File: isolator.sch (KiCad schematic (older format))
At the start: 0 parts

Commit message: Added library for project specific symbols
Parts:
- added U?: Si8640BA-B-IU, Package_SO:QSOP-16_3.9x4.9mm_P0.635mm, symbol Isolator:Si8640BA-B-IU
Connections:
- net labels added: IN1, IN2, IN3, IN4, IN5, IN6, OUT1, OUT2, OUT3, OUT4, OUT5, OUT6
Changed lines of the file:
@@
 Comment4 ""
 $EndDescr
+$Comp
+L Isolator:Si8640BA-B-IU U?
+U 1 1 5BCC634E
+P 5350 3650
+F 0 "U?" H 5350 4317 50  0000 C CNN
+F 1 "Si8640BA-B-IU" H 5350 4226 50  0000 C CNN
+F 2 "Package_SO:QSOP-16_3.9x4.9mm_P0.635mm" H 5350 3100 50  0001 C CIN
+F 3 "https://www.silabs.com/documents/public/data-sheets/si864x-datasheet.pdf" H 5350 4050 50  0001 C CNN
+	1    5350 3650
+	1    0    0    -1
+$EndComp
+Text HLabel 3650 3350 0    50   Input ~ 0
+IN1
+Text HLabel 3650 3450 0    50   Input ~ 0
+IN2
+Text HLabel 3650 3550 0    50   Input ~ 0
+IN3
+Text HLabel 3650 3650 0    50   Input ~ 0
+IN4
+Text HLabel 3650 3750 0    50   Input ~ 0
+IN5
+Text HLabel 3650 3850 0    50   Input ~ 0
+IN6
+Text HLabel 6850 3250 2    50   Output ~ 0
+OUT1
+Text HLabel 6850 3350 2    50   Output ~ 0
+OUT2
+Text HLabel 6850 3450 2    50   Output ~ 0
+OUT3
+Text HLabel 6850 3550 2    50   Output ~ 0
+OUT4
+Text HLabel 6850 3650 2    50   Output ~ 0
+OUT5
+Text HLabel 6850 3750 2    50   Output ~ 0
+OUT6
 $EndSCHEMATC

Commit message: Added isolators and RJ-45 connectors
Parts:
- removed U?: Si8640BA-B-IU, Package_SO:QSOP-16_3.9x4.9mm_P0.635mm, symbol Isolator:Si8640BA-B-IU
- added U?: Si8640BB-B-IS1, Package_SO:SOIC-16_3.9x9.9mm_P1.27mm, symbol Isolator:Si8640BB-B-IS1
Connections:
- net labels added: +3V3, +5V, GNDREF
- net labels removed: IN5, IN6, OUT5, OUT6
- wire segments 0 -> 18
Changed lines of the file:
@@
 $Descr A4 11693 8268
 encoding utf-8
-Sheet 3 5
+Sheet 6 8
 Title ""
 Date ""
@@
 Comment4 ""
 $EndDescr
+Text HLabel 4400 3400 0    50   Input ~ 0
+IN1
+Text HLabel 4400 3500 0    50   Input ~ 0
+IN2
+Text HLabel 4400 3600 0    50   Input ~ 0
+IN3
+Text HLabel 4400 3700 0    50   Input ~ 0
+IN4
+Text HLabel 5950 3400 2    50   Output ~ 0
+OUT1
+Text HLabel 5950 3500 2    50   Output ~ 0
+OUT2
+Text HLabel 5950 3600 2    50   Output ~ 0
+OUT3
+Text HLabel 5950 3700 2    50   Output ~ 0
+OUT4
 $Comp
-L Isolator:Si8640BA-B-IU U?
-U 1 1 5BCC634E
-P 5350 3650
-F 0 "U?" H 5350 4317 50  0000 C CNN
-F 1 "Si8640BA-B-IU" H 5350 4226 50  0000 C CNN
-F 2 "Package_SO:QSOP-16_3.9x4.9mm_P0.635mm" H 5350 3100 50  0001 C CIN
-F 3 "https://www.silabs.com/documents/public/data-sheets/si864x-datasheet.pdf" H 5350 4050 50  0001 C CNN
-	1    5350 3650
+L Isolator:Si8640BB-B-IS1 U?
+U 1 1 5BCC7CBC
+P 5200 3500
+AR Path="/5BCC578B/5BCC7CBC" Ref="U?"  Part="1"
+AR Path="/5BCC79AE/5BCC7CBC" Ref="U?"  Part="1"
+F 0 "U?" H 5200 4167 50  0000 C CNN
+F 1 "Si8640BB-B-IS1" H 5200 4076 50  0000 C CNN
+F 2 "Package_SO:SOIC-16_3.9x9.9mm_P1.27mm" H 5200 2950 50  0001 C CIN
+F 3 "https://www.silabs.com/documents/public/data-sheets/si864x-datasheet.pdf" H 5200 3900 50  0001 C CNN
+	1    5200 3500
 	1    0    0    -1
 $EndComp
-Text HLabel 3650 3350 0    50   Input ~ 0
-IN1
-Text HLabel 3650 3450 0    50   Input ~ 0
-IN2
-Text HLabel 3650 3550 0    50   Input ~ 0
-IN3
-Text HLabel 3650 3650 0    50   Input ~ 0
-IN4
-Text HLabel 3650 3750 0    50   Input ~ 0
-IN5
-Text HLabel 3650 3850 0    50   Input ~ 0
-IN6
-Text HLabel 6850 3250 2    50   Output ~ 0
-OUT1
-Text HLabel 6850 3350 2    50   Output ~ 0
-OUT2
-Text HLabel 6850 3450 2    50   Output ~ 0
-OUT3
-Text HLabel 6850 3550 2    50   Output ~ 0
-OUT4
-Text HLabel 6850 3650 2    50   Output ~ 0
-OUT5
-Text HLabel 6850 3750 2    50   Output ~ 0
-OUT6
+$Comp
+L power:GNDREF #PWR?
+U 1 1 5BCC7D47
+P 4650 4100
+AR Path="/5BCC578B/5BCC7D47" Ref="#PWR?"  Part="1"
+AR Path="/5BCC79AE/5BCC7D47" Ref="#PWR?"  Part="1"
+F 0 "#PWR?" H 4650 3850 50  0001 C CNN
+F 1 "GNDREF" H 4655 3927 50  0000 C CNN
+F 2 "" H 4650 4100 50  0001 C CNN
+F 3 "" H 4650 4100 50  0001 C CNN
+	1    4650 4100
+	1    0    0    -1
+$EndComp
+$Comp
+L power:GNDREF #PWR?
+U 1 1 5BCC7D5B
+P 5750 4100
+AR Path="/5BCC578B/5BCC7D5B" Ref="#PWR?"  Part="1"
+AR Path="/5BCC79AE/5BCC7D5B" Ref="#PWR?"  Part="1"
+F 0 "#PWR?" H 5750 3850 50  0001 C CNN
+F 1 "GNDREF" H 5755 3927 50  0000 C CNN
+F 2 "" H 5750 4100 50  0001 C CNN
+F 3 "" H 5750 4100 50  0001 C CNN
+	1    5750 4100
+	1    0    0    -1
+$EndComp
+$Comp
+L power:+3V3 #PWR?
+U 1 1 5BCC7DB8
+P 4650 2950
+AR Path="/5BCC578B/5BCC7DB8" Ref="#PWR?"  Part="1"
+AR Path="/5BCC79AE/5BCC7DB8" Ref="#PWR?"  Part="1"
+F 0 "#PWR?" H 4650 2800 50  0001 C CNN
+F 1 "+3V3" H 4665 3123 50  0000 C CNN
+F 2 "" H 4650 2950 50  0001 C CNN
+F 3 "" H 4650 2950 50  0001 C CNN
+	1    4650 2950
+	1    0    0    -1
+$EndComp
+$Comp
+L power:+5V #PWR?
+U 1 1 5BCC7E07
+P 5750 2950
+AR Path="/5BCC578B/5BCC7E07" Ref="#PWR?"  Part="1"
+AR Path="/5BCC79AE/5BCC7E07" Ref="#PWR?"  Part="1"
+F 0 "#PWR?" H 5750 2800 50  0001 C CNN
+F 1 "+5V" H 5765 3123 50  0000 C CNN
+F 2 "" H 5750 2950 50  0001 C CNN
+F 3 "" H 5750 2950 50  0001 C CNN
+	1    5750 2950
+	1    0    0    -1
+$EndComp
+Wire Wire Line
+	5600 3100 5750 3100
+Wire Wire Line
+	5600 3200 5750 3200
+Wire Wire Line
+	5750 3200 5750 3100
+Connection ~ 5750 3100
+Wire Wire Line
+	5600 3400 5950 3400
+Wire Wire Line
+	5950 3500 5600 3500
+Wire Wire Line
+	5600 3600 5950 3600
+Wire Wire Line
+	5600 3700 5950 3700
+Wire Wire Line
+	5600 3900 5750 3900
+Wire Wire Line
+	5750 3900 5750 4100
+Wire Wire Line
+	4800 3100 4650 3100
+Wire Wire Line
+	4650 3100 4650 2950
+Wire Wire Line
+	4650 4100 4650 3900
+Wire Wire Line
+	4650 3900 4800 3900
+Wire Wire Line
+	4800 3700 4400 3700
+Wire Wire Line
+	4400 3600 4800 3600
+Wire Wire Line
+	4800 3500 4400 3500
+Wire Wire Line
+	4400 3400 4800 3400
+Wire Wire Line
+	5750 2950 5750 3100
 $EndSCHEMATC

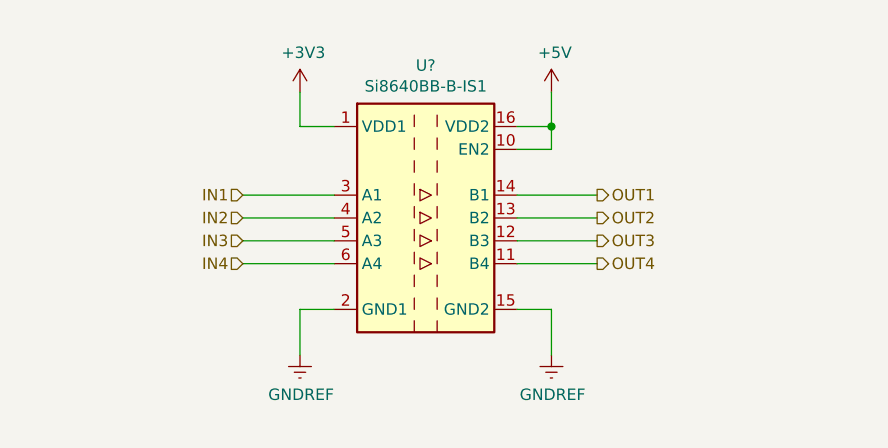
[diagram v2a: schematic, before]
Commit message: Added charge pump IC REG71050
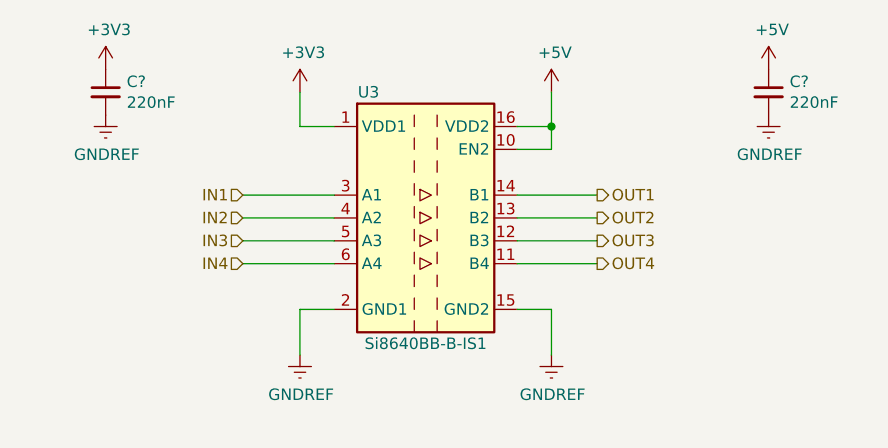
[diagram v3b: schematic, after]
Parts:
- added C? (x2): 220nF, symbol Device:C_Small
- gave numbers to parts that had none: 1
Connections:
- net +3V3: now also C?.1
- net +5V: now also C?.1
- net GNDREF: now also C?.2, C?.2
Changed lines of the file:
@@
 $Descr A4 11693 8268
 encoding utf-8
-Sheet 6 8
+Sheet 6 11
 Title ""
 Date ""
@@
 OUT4
 $Comp
-L Isolator:Si8640BB-B-IS1 U?
+L Isolator:Si8640BB-B-IS1 U1
 U 1 1 5BCC7CBC
 P 5200 3500
-AR Path="/5BCC578B/5BCC7CBC" Ref="U?"  Part="1"
-AR Path="/5BCC79AE/5BCC7CBC" Ref="U?"  Part="1"
-F 0 "U?" H 5200 4167 50  0000 C CNN
-F 1 "Si8640BB-B-IS1" H 5200 4076 50  0000 C CNN
+AR Path="/5BCC578B/5BCC7CBC" Ref="U1"  Part="1"
+AR Path="/5BCC79AE/5BCC7CBC" Ref="U3"  Part="1"
+AR Path="/5BCC7A96/5BCC7CBC" Ref="U2"  Part="1"
+AR Path="/5BCC8BB7/5BCC7CBC" Ref="U4"  Part="1"
+F 0 "U3" H 4950 4050 50  0000 C CNN
+F 1 "Si8640BB-B-IS1" H 5200 2950 50  0000 C CNN
 F 2 "Package_SO:SOIC-16_3.9x9.9mm_P1.27mm" H 5200 2950 50  0001 C CIN
 F 3 "https://www.silabs.com/documents/public/data-sheets/si864x-datasheet.pdf" H 5200 3900 50  0001 C CNN
@@
 $EndComp
 $Comp
-L power:GNDREF #PWR?
+L power:GNDREF #PWR0105
 U 1 1 5BCC7D47
 P 4650 4100
-AR Path="/5BCC578B/5BCC7D47" Ref="#PWR?"  Part="1"
-AR Path="/5BCC79AE/5BCC7D47" Ref="#PWR?"  Part="1"
-F 0 "#PWR?" H 4650 3850 50  0001 C CNN
+AR Path="/5BCC578B/5BCC7D47" Ref="#PWR0105"  Part="1"
+AR Path="/5BCC79AE/5BCC7D47" Ref="#PWR0118"  Part="1"
+AR Path="/5BCC7A96/5BCC7D47" Ref="#PWR0114"  Part="1"
+AR Path="/5BCC8BB7/5BCC7D47" Ref="#PWR0122"  Part="1"
+F 0 "#PWR0118" H 4650 3850 50  0001 C CNN
 F 1 "GNDREF" H 4655 3927 50  0000 C CNN
 F 2 "" H 4650 4100 50  0001 C CNN
@@
 $EndComp
 $Comp
-L power:GNDREF #PWR?
+L power:GNDREF #PWR0106
 U 1 1 5BCC7D5B
 P 5750 4100
-AR Path="/5BCC578B/5BCC7D5B" Ref="#PWR?"  Part="1"
-AR Path="/5BCC79AE/5BCC7D5B" Ref="#PWR?"  Part="1"
-F 0 "#PWR?" H 5750 3850 50  0001 C CNN
+AR Path="/5BCC578B/5BCC7D5B" Ref="#PWR0106"  Part="1"
+AR Path="/5BCC79AE/5BCC7D5B" Ref="#PWR0119"  Part="1"
+AR Path="/5BCC7A96/5BCC7D5B" Ref="#PWR0115"  Part="1"
+AR Path="/5BCC8BB7/5BCC7D5B" Ref="#PWR0123"  Part="1"
+F 0 "#PWR0119" H 5750 3850 50  0001 C CNN
 F 1 "GNDREF" H 5755 3927 50  0000 C CNN
 F 2 "" H 5750 4100 50  0001 C CNN
@@
 $EndComp
 $Comp
-L power:+3V3 #PWR?
+L power:+3V3 #PWR0107
 U 1 1 5BCC7DB8
 P 4650 2950
-AR Path="/5BCC578B/5BCC7DB8" Ref="#PWR?"  Part="1"
-AR Path="/5BCC79AE/5BCC7DB8" Ref="#PWR?"  Part="1"
-F 0 "#PWR?" H 4650 2800 50  0001 C CNN
+AR Path="/5BCC578B/5BCC7DB8" Ref="#PWR0107"  Part="1"
+AR Path="/5BCC79AE/5BCC7DB8" Ref="#PWR0120"  Part="1"
+AR Path="/5BCC7A96/5BCC7DB8" Ref="#PWR0116"  Part="1"
+AR Path="/5BCC8BB7/5BCC7DB8" Ref="#PWR0124"  Part="1"
+F 0 "#PWR0120" H 4650 2800 50  0001 C CNN
 F 1 "+3V3" H 4665 3123 50  0000 C CNN
 F 2 "" H 4650 2950 50  0001 C CNN
@@
 $EndComp
 $Comp
-L power:+5V #PWR?
+L power:+5V #PWR0108
 U 1 1 5BCC7E07
 P 5750 2950
-AR Path="/5BCC578B/5BCC7E07" Ref="#PWR?"  Part="1"
-AR Path="/5BCC79AE/5BCC7E07" Ref="#PWR?"  Part="1"
-F 0 "#PWR?" H 5750 2800 50  0001 C CNN
+AR Path="/5BCC578B/5BCC7E07" Ref="#PWR0108"  Part="1"
+AR Path="/5BCC79AE/5BCC7E07" Ref="#PWR0121"  Part="1"
+AR Path="/5BCC7A96/5BCC7E07" Ref="#PWR0117"  Part="1"
+AR Path="/5BCC8BB7/5BCC7E07" Ref="#PWR0125"  Part="1"
+F 0 "#PWR0121" H 5750 2800 50  0001 C CNN
 F 1 "+5V" H 5765 3123 50  0000 C CNN
 F 2 "" H 5750 2950 50  0001 C CNN
@@
 Wire Wire Line
 	5750 2950 5750 3100
+$Comp
+L power:+3V3 #PWR?
+U 1 1 5BCCF224
+P 3800 2850
+AR Path="/5BCC578B/5BCCF224" Ref="#PWR?"  Part="1"
+AR Path="/5BCC79AE/5BCCF224" Ref="#PWR?"  Part="1"
+AR Path="/5BCC7A96/5BCCF224" Ref="#PWR?"  Part="1"
+AR Path="/5BCC8BB7/5BCCF224" Ref="#PWR?"  Part="1"
+F 0 "#PWR?" H 3800 2700 50  0001 C CNN
+F 1 "+3V3" H 3815 3023 50  0000 C CNN
+F 2 "" H 3800 2850 50  0001 C CNN
+F 3 "" H 3800 2850 50  0001 C CNN
+	1    3800 2850
+	1    0    0    -1
+$EndComp
+$Comp
+L Device:C_Small C?
+U 1 1 5BCCF242
+P 3800 2950
+AR Path="/5BCC578B/5BCCF242" Ref="C?"  Part="1"
+AR Path="/5BCC79AE/5BCCF242" Ref="C?"  Part="1"
+F 0 "C?" H 3892 2996 50  0000 L CNN
+F 1 "220nF" H 3892 2905 50  0000 L CNN
+F 2 "" H 3800 2950 50  0001 C CNN
+F 3 "~" H 3800 2950 50  0001 C CNN
+	1    3800 2950
+	1    0    0    -1
+$EndComp
+$Comp
+L power:GNDREF #PWR?
+U 1 1 5BCCF276
+P 3800 3050
+AR Path="/5BCC578B/5BCCF276" Ref="#PWR?"  Part="1"
+AR Path="/5BCC79AE/5BCCF276" Ref="#PWR?"  Part="1"
+F 0 "#PWR?" H 3800 2800 50  0001 C CNN
+F 1 "GNDREF" H 3805 2877 50  0000 C CNN
+F 2 "" H 3800 3050 50  0001 C CNN
+F 3 "" H 3800 3050 50  0001 C CNN
+	1    3800 3050
+	1    0    0    -1
+$EndComp
+$Comp
+L Device:C_Small C?
+U 1 1 5BCCF2B7
+P 6700 2950
+AR Path="/5BCC578B/5BCCF2B7" Ref="C?"  Part="1"
+AR Path="/5BCC79AE/5BCCF2B7" Ref="C?"  Part="1"
+F 0 "C?" H 6792 2996 50  0000 L CNN
+F 1 "220nF" H 6792 2905 50  0000 L CNN
+F 2 "" H 6700 2950 50  0001 C CNN
+F 3 "~" H 6700 2950 50  0001 C CNN
+	1    6700 2950
+	1    0    0    -1
+$EndComp
+$Comp
+L power:+5V #PWR?
+U 1 1 5BCCF324
+P 6700 2850
+AR Path="/5BCC578B/5BCCF324" Ref="#PWR?"  Part="1"
+AR Path="/5BCC79AE/5BCCF324" Ref="#PWR?"  Part="1"
+AR Path="/5BCC7A96/5BCCF324" Ref="#PWR?"  Part="1"
+AR Path="/5BCC8BB7/5BCCF324" Ref="#PWR?"  Part="1"
+F 0 "#PWR?" H 6700 2700 50  0001 C CNN
+F 1 "+5V" H 6715 3023 50  0000 C CNN
+F 2 "" H 6700 2850 50  0001 C CNN
+F 3 "" H 6700 2850 50  0001 C CNN
+	1    6700 2850
+	1    0    0    -1
+$EndComp
+$Comp
+L power:GNDREF #PWR?
+U 1 1 5BCCF348
+P 6700 3050
+AR Path="/5BCC578B/5BCCF348" Ref="#PWR?"  Part="1"
+AR Path="/5BCC79AE/5BCCF348" Ref="#PWR?"  Part="1"
+F 0 "#PWR?" H 6700 2800 50  0001 C CNN
+F 1 "GNDREF" H 6705 2877 50  0000 C CNN
+F 2 "" H 6700 3050 50  0001 C CNN
+F 3 "" H 6700 3050 50  0001 C CNN
+	1    6700 3050
+	1    0    0    -1
+$EndComp
 $EndSCHEMATC

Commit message: Assigned footprints
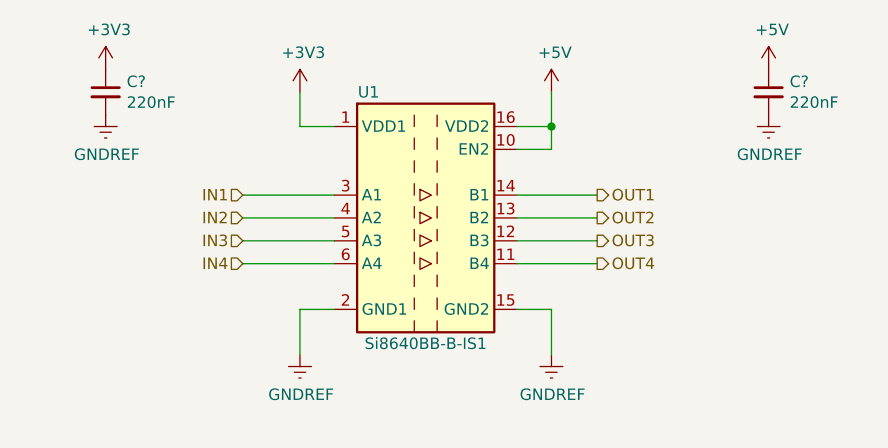
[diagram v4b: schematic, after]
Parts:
- C? (x2): footprint (none) -> Capacitor_SMD:C_0805_2012Metric_Pad1.15x1.40mm_HandSolder
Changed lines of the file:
@@
 $Descr A4 11693 8268
 encoding utf-8
-Sheet 6 11
+Sheet 3 11
 Title ""
 Date ""
@@
 AR Path="/5BCC7A96/5BCC7CBC" Ref="U2"  Part="1"
 AR Path="/5BCC8BB7/5BCC7CBC" Ref="U4"  Part="1"
-F 0 "U3" H 4950 4050 50  0000 C CNN
+F 0 "U1" H 4950 4050 50  0000 C CNN
 F 1 "Si8640BB-B-IS1" H 5200 2950 50  0000 C CNN
 F 2 "Package_SO:SOIC-16_3.9x9.9mm_P1.27mm" H 5200 2950 50  0001 C CIN
@@
 AR Path="/5BCC7A96/5BCC7D47" Ref="#PWR0114"  Part="1"
 AR Path="/5BCC8BB7/5BCC7D47" Ref="#PWR0122"  Part="1"
-F 0 "#PWR0118" H 4650 3850 50  0001 C CNN
+F 0 "#PWR0105" H 4650 3850 50  0001 C CNN
 F 1 "GNDREF" H 4655 3927 50  0000 C CNN
 F 2 "" H 4650 4100 50  0001 C CNN
@@
 AR Path="/5BCC7A96/5BCC7D5B" Ref="#PWR0115"  Part="1"
 AR Path="/5BCC8BB7/5BCC7D5B" Ref="#PWR0123"  Part="1"
-F 0 "#PWR0119" H 5750 3850 50  0001 C CNN
+F 0 "#PWR0106" H 5750 3850 50  0001 C CNN
 F 1 "GNDREF" H 5755 3927 50  0000 C CNN
 F 2 "" H 5750 4100 50  0001 C CNN
@@
 AR Path="/5BCC7A96/5BCC7DB8" Ref="#PWR0116"  Part="1"
 AR Path="/5BCC8BB7/5BCC7DB8" Ref="#PWR0124"  Part="1"
-F 0 "#PWR0120" H 4650 2800 50  0001 C CNN
+F 0 "#PWR0107" H 4650 2800 50  0001 C CNN
 F 1 "+3V3" H 4665 3123 50  0000 C CNN
 F 2 "" H 4650 2950 50  0001 C CNN
@@
 AR Path="/5BCC7A96/5BCC7E07" Ref="#PWR0117"  Part="1"
 AR Path="/5BCC8BB7/5BCC7E07" Ref="#PWR0125"  Part="1"
-F 0 "#PWR0121" H 5750 2800 50  0001 C CNN
+F 0 "#PWR0108" H 5750 2800 50  0001 C CNN
 F 1 "+5V" H 5765 3123 50  0000 C CNN
 F 2 "" H 5750 2950 50  0001 C CNN
@@
 F 0 "C?" H 3892 2996 50  0000 L CNN
 F 1 "220nF" H 3892 2905 50  0000 L CNN
-F 2 "" H 3800 2950 50  0001 C CNN
+F 2 "Capacitor_SMD:C_0805_2012Metric_Pad1.15x1.40mm_HandSolder" H 3800 2950 50  0001 C CNN
 F 3 "~" H 3800 2950 50  0001 C CNN
 	1    3800 2950
@@
 F 0 "C?" H 6792 2996 50  0000 L CNN
 F 1 "220nF" H 6792 2905 50  0000 L CNN
-F 2 "" H 6700 2950 50  0001 C CNN
+F 2 "Capacitor_SMD:C_0805_2012Metric_Pad1.15x1.40mm_HandSolder" H 6700 2950 50  0001 C CNN
 F 3 "~" H 6700 2950 50  0001 C CNN
 	1    6700 2950

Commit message: Began layouting
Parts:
- gave numbers to parts that had none: 2
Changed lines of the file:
@@
 AR Path="/5BCC7A96/5BCC7CBC" Ref="U2"  Part="1"
 AR Path="/5BCC8BB7/5BCC7CBC" Ref="U4"  Part="1"
-F 0 "U1" H 4950 4050 50  0000 C CNN
+F 0 "U4" H 4950 4050 50  0000 C CNN
 F 1 "Si8640BB-B-IS1" H 5200 2950 50  0000 C CNN
 F 2 "Package_SO:SOIC-16_3.9x9.9mm_P1.27mm" H 5200 2950 50  0001 C CIN
@@
 AR Path="/5BCC7A96/5BCC7D47" Ref="#PWR0114"  Part="1"
 AR Path="/5BCC8BB7/5BCC7D47" Ref="#PWR0122"  Part="1"
-F 0 "#PWR0105" H 4650 3850 50  0001 C CNN
+F 0 "#PWR0122" H 4650 3850 50  0001 C CNN
 F 1 "GNDREF" H 4655 3927 50  0000 C CNN
 F 2 "" H 4650 4100 50  0001 C CNN
@@
 AR Path="/5BCC7A96/5BCC7D5B" Ref="#PWR0115"  Part="1"
 AR Path="/5BCC8BB7/5BCC7D5B" Ref="#PWR0123"  Part="1"
-F 0 "#PWR0106" H 5750 3850 50  0001 C CNN
+F 0 "#PWR0123" H 5750 3850 50  0001 C CNN
 F 1 "GNDREF" H 5755 3927 50  0000 C CNN
 F 2 "" H 5750 4100 50  0001 C CNN
@@
 AR Path="/5BCC7A96/5BCC7DB8" Ref="#PWR0116"  Part="1"
 AR Path="/5BCC8BB7/5BCC7DB8" Ref="#PWR0124"  Part="1"
-F 0 "#PWR0107" H 4650 2800 50  0001 C CNN
+F 0 "#PWR0124" H 4650 2800 50  0001 C CNN
 F 1 "+3V3" H 4665 3123 50  0000 C CNN
 F 2 "" H 4650 2950 50  0001 C CNN
@@
 AR Path="/5BCC7A96/5BCC7E07" Ref="#PWR0117"  Part="1"
 AR Path="/5BCC8BB7/5BCC7E07" Ref="#PWR0125"  Part="1"
-F 0 "#PWR0108" H 5750 2800 50  0001 C CNN
+F 0 "#PWR0125" H 5750 2800 50  0001 C CNN
 F 1 "+5V" H 5765 3123 50  0000 C CNN
 F 2 "" H 5750 2950 50  0001 C CNN
@@
 	5750 2950 5750 3100
 $Comp
-L power:+3V3 #PWR?
+L power:+3V3 #PWR01
 U 1 1 5BCCF224
 P 3800 2850
-AR Path="/5BCC578B/5BCCF224" Ref="#PWR?"  Part="1"
-AR Path="/5BCC79AE/5BCCF224" Ref="#PWR?"  Part="1"
-AR Path="/5BCC7A96/5BCCF224" Ref="#PWR?"  Part="1"
-AR Path="/5BCC8BB7/5BCCF224" Ref="#PWR?"  Part="1"
-F 0 "#PWR?" H 3800 2700 50  0001 C CNN
+AR Path="/5BCC578B/5BCCF224" Ref="#PWR01"  Part="1"
+AR Path="/5BCC79AE/5BCCF224" Ref="#PWR09"  Part="1"
+AR Path="/5BCC7A96/5BCCF224" Ref="#PWR05"  Part="1"
+AR Path="/5BCC8BB7/5BCCF224" Ref="#PWR013"  Part="1"
+F 0 "#PWR013" H 3800 2700 50  0001 C CNN
 F 1 "+3V3" H 3815 3023 50  0000 C CNN
 F 2 "" H 3800 2850 50  0001 C CNN
@@
 $EndComp
 $Comp
-L Device:C_Small C?
+L Device:C_Small C4
 U 1 1 5BCCF242
 P 3800 2950
-AR Path="/5BCC578B/5BCCF242" Ref="C?"  Part="1"
-AR Path="/5BCC79AE/5BCCF242" Ref="C?"  Part="1"
-F 0 "C?" H 3892 2996 50  0000 L CNN
+AR Path="/5BCC578B/5BCCF242" Ref="C4"  Part="1"
+AR Path="/5BCC79AE/5BCCF242" Ref="C8"  Part="1"
+AR Path="/5BCC7A96/5BCCF242" Ref="C6"  Part="1"
+AR Path="/5BCC8BB7/5BCCF242" Ref="C10"  Part="1"
+F 0 "C10" H 3892 2996 50  0000 L CNN
 F 1 "220nF" H 3892 2905 50  0000 L CNN
 F 2 "Capacitor_SMD:C_0805_2012Metric_Pad1.15x1.40mm_HandSolder" H 3800 2950 50  0001 C CNN
@@
 $EndComp
 $Comp
-L power:GNDREF #PWR?
+L power:GNDREF #PWR02
 U 1 1 5BCCF276
 P 3800 3050
-AR Path="/5BCC578B/5BCCF276" Ref="#PWR?"  Part="1"
-AR Path="/5BCC79AE/5BCCF276" Ref="#PWR?"  Part="1"
-F 0 "#PWR?" H 3800 2800 50  0001 C CNN
+AR Path="/5BCC578B/5BCCF276" Ref="#PWR02"  Part="1"
+AR Path="/5BCC79AE/5BCCF276" Ref="#PWR010"  Part="1"
+AR Path="/5BCC7A96/5BCCF276" Ref="#PWR06"  Part="1"
+AR Path="/5BCC8BB7/5BCCF276" Ref="#PWR014"  Part="1"
+F 0 "#PWR014" H 3800 2800 50  0001 C CNN
 F 1 "GNDREF" H 3805 2877 50  0000 C CNN
 F 2 "" H 3800 3050 50  0001 C CNN
@@
 $EndComp
 $Comp
-L Device:C_Small C?
+L Device:C_Small C5
 U 1 1 5BCCF2B7
 P 6700 2950
-AR Path="/5BCC578B/5BCCF2B7" Ref="C?"  Part="1"
-AR Path="/5BCC79AE/5BCCF2B7" Ref="C?"  Part="1"
-F 0 "C?" H 6792 2996 50  0000 L CNN
+AR Path="/5BCC578B/5BCCF2B7" Ref="C5"  Part="1"
+AR Path="/5BCC79AE/5BCCF2B7" Ref="C9"  Part="1"
+AR Path="/5BCC7A96/5BCCF2B7" Ref="C7"  Part="1"
+AR Path="/5BCC8BB7/5BCCF2B7" Ref="C11"  Part="1"
+F 0 "C11" H 6792 2996 50  0000 L CNN
 F 1 "220nF" H 6792 2905 50  0000 L CNN
 F 2 "Capacitor_SMD:C_0805_2012Metric_Pad1.15x1.40mm_HandSolder" H 6700 2950 50  0001 C CNN
@@
 $EndComp
 $Comp
-L power:+5V #PWR?
+L power:+5V #PWR03
 U 1 1 5BCCF324
 P 6700 2850
-AR Path="/5BCC578B/5BCCF324" Ref="#PWR?"  Part="1"
-AR Path="/5BCC79AE/5BCCF324" Ref="#PWR?"  Part="1"
-AR Path="/5BCC7A96/5BCCF324" Ref="#PWR?"  Part="1"
-AR Path="/5BCC8BB7/5BCCF324" Ref="#PWR?"  Part="1"
-F 0 "#PWR?" H 6700 2700 50  0001 C CNN
+AR Path="/5BCC578B/5BCCF324" Ref="#PWR03"  Part="1"
+AR Path="/5BCC79AE/5BCCF324" Ref="#PWR011"  Part="1"
+AR Path="/5BCC7A96/5BCCF324" Ref="#PWR07"  Part="1"
+AR Path="/5BCC8BB7/5BCCF324" Ref="#PWR015"  Part="1"
+F 0 "#PWR015" H 6700 2700 50  0001 C CNN
 F 1 "+5V" H 6715 3023 50  0000 C CNN
 F 2 "" H 6700 2850 50  0001 C CNN
@@
 $EndComp
 $Comp
-L power:GNDREF #PWR?
+L power:GNDREF #PWR04
 U 1 1 5BCCF348
 P 6700 3050
-AR Path="/5BCC578B/5BCCF348" Ref="#PWR?"  Part="1"
-AR Path="/5BCC79AE/5BCCF348" Ref="#PWR?"  Part="1"
-F 0 "#PWR?" H 6700 2800 50  0001 C CNN
+AR Path="/5BCC578B/5BCCF348" Ref="#PWR04"  Part="1"
+AR Path="/5BCC79AE/5BCCF348" Ref="#PWR012"  Part="1"
+AR Path="/5BCC7A96/5BCCF348" Ref="#PWR08"  Part="1"
+AR Path="/5BCC8BB7/5BCCF348" Ref="#PWR016"  Part="1"
+F 0 "#PWR016" H 6700 2800 50  0001 C CNN
 F 1 "GNDREF" H 6705 2877 50  0000 C CNN
 F 2 "" H 6700 3050 50  0001 C CNN
